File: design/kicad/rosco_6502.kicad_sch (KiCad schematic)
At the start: 54 parts, among them IC1 W65C02SxP, IC2 ATF22V10C-7PX, IC3 XR68C681CJTR-F, IC4 NE555P, IC5 ATF22V10C-7PX, J1 UART_A, J2 UART_B, J3 Conn_01x06, J4 Conn_01x01_Male, J5 Conn_02x18_Odd_Even, J6 Conn_01x02_Male, Q1 3.6864MHz, SW1 SW_DPST, U1 AS6C4008-55PCN, U2 AS6C62256-55PCN, U3 AT28C64B-15PU, U4 74HCT174, X1 14MHz

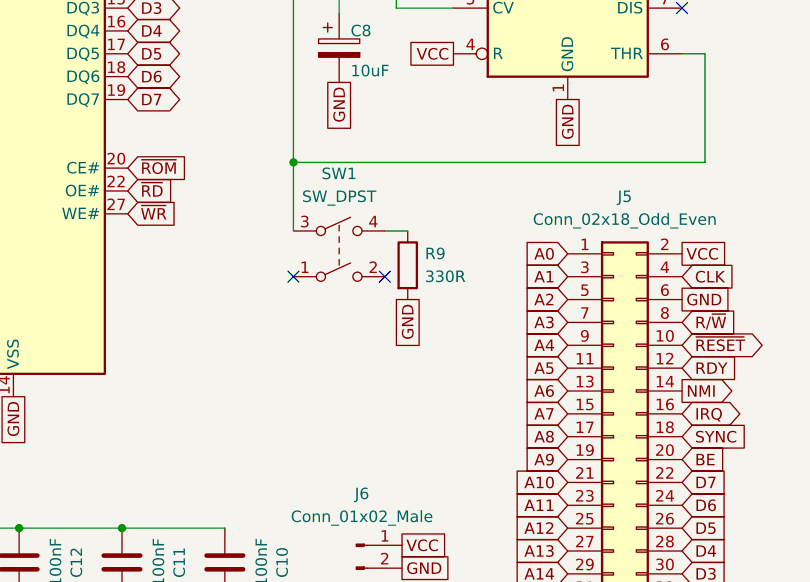
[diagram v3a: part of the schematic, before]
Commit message: Fix incorrect button symbol
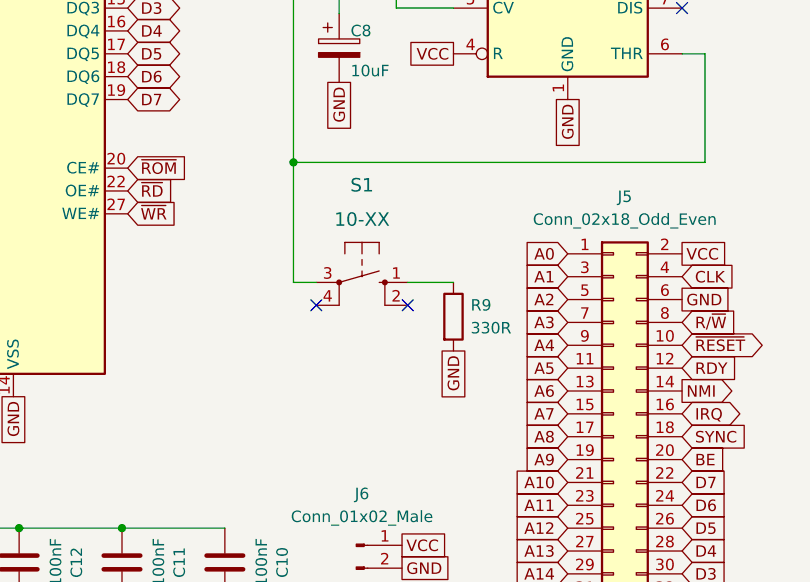
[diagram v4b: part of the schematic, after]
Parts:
- removed SW1: SW_DPST, rosco_6502:B3F-10XX, symbol Switch:SW_DPST
- added S1: 10-XX, rosco_6502:B3F-10XX, symbol rosco_6502:10-XX
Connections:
- net at C8.1, IC4.2 (TR), IC4.6 (THR)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: now also S1.3 (P)
- net at R9.1: now also S1.1 (S)
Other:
- moved on the sheet: R9
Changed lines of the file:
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@@
   (junction (at 195.58 92.71) (diameter 0) (color 0 0 0 0)
   )
-  (no_connect (at 226.06 64.77))
-  (no_connect (at 236.22 64.77))
+  (no_connect (at 228.6 67.945))
+  (no_connect (at 238.76 67.945))
   (no_connect (at 269.24 34.925))
   (no_connect (at 106.68 125.095))
@@
     (stroke (width 0) (type default) (color 0 0 0 0))
   )
-  (wire (pts (xy 226.06 59.69) (xy 226.06 52.07))
+  (wire (pts (xy 226.06 52.07) (xy 226.06 65.405))
     (stroke (width 0) (type default) (color 0 0 0 0))
   )
@@
     (stroke (width 0) (type default) (color 0 0 0 0))
   )
+  (wire (pts (xy 228.6 65.405) (xy 226.06 65.405))
+    (stroke (width 0) (type default) (color 0 0 0 0))
+  )
   (wire (pts (xy 271.78 52.07) (xy 226.06 52.07))
     (stroke (width 0) (type default) (color 0 0 0 0))
@@
     (stroke (width 0) (type default) (color 0 0 0 0))
   )
-  (wire (pts (xy 236.22 59.69) (xy 238.76 59.69))
+  (wire (pts (xy 238.76 65.405) (xy 243.84 65.405))
     (stroke (width 0) (type default) (color 0 0 0 0))
   )
@@
     )
   )
-  (global_label "GND" (shape passive) (at 238.76 67.31 270) (fields_autoplaced)
+  (global_label "GND" (shape passive) (at 243.84 73.025 270) (fields_autoplaced)
     (effects (font (size 1.27 1.27)) (justify right))
-    (property "Intersheet References" "${INTERSHEET_REFS}" (id 0) (at 238.6806 73.5936 90)
+    (property "Intersheet References" "${INTERSHEET_REFS}" (id 0) (at 243.7606 79.3086 90)
       (effects (font (size 1.27 1.27)) (justify right) hide)
     )
@@
     (pin "2")
   )
-  (symbol (lib_id "Switch:SW_DPST") (at 231.14 62.23 0) (unit 1)
-    (in_bom yes) (on_board yes) (fields_autoplaced)
-    (property "Reference" "SW1" (id 0) (at 231.14 53.34 0))
-    (property "Value" "SW_DPST" (id 1) (at 231.14 55.88 0))
-    (property "Footprint" "rosco_6502:B3F-10XX" (id 2) (at 231.14 62.23 0)
-      (effects (font (size 1.27 1.27)) hide)
-    )
-    (property "Datasheet" "~" (id 3) (at 231.14 62.23 0)
-      (effects (font (size 1.27 1.27)) hide)
-    )
-    (pin "1")
-    (pin "2")
-    (pin "3")
-    (pin "4")
-  )
   (symbol (lib_id "Connector_Generic:Conn_02x18_Odd_Even") (at 261.62 82.55 0) (unit 1)
     (in_bom yes) (on_board yes) (fields_autoplaced)
@@
     (pin "6")
   )
-  (symbol (lib_id "Device:R") (at 238.76 63.5 0) (unit 1)
+  (symbol (lib_id "Device:R") (at 243.84 69.215 0) (unit 1)
     (in_bom yes) (on_board yes)
-    (property "Reference" "R9" (id 0) (at 240.665 62.23 0)
+    (property "Reference" "R9" (id 0) (at 245.745 67.945 0)
       (effects (font (size 1.27 1.27)) (justify left))
     )
-    (property "Value" "330R" (id 1) (at 240.665 64.77 0)
+    (property "Value" "330R" (id 1) (at 245.745 70.485 0)
       (effects (font (size 1.27 1.27)) (justify left))
     )
-    (property "Footprint" "Resistor_THT:R_Axial_DIN0207_L6.3mm_D2.5mm_P10.16mm_Horizontal" (id 2) (at 236.982 63.5 90)
+    (property "Footprint" "Resistor_THT:R_Axial_DIN0207_L6.3mm_D2.5mm_P10.16mm_Horizontal" (id 2) (at 242.062 69.215 90)
       (effects (font (size 1.27 1.27)) hide)
     )
-    (property "Datasheet" "~" (id 3) (at 238.76 63.5 0)
+    (property "Datasheet" "~" (id 3) (at 243.84 69.215 0)
       (effects (font (size 1.27 1.27)) hide)
     )
@@
     (pin "2")
   )
+  (symbol (lib_id "rosco_6502:10-XX") (at 233.68 65.405 270) (unit 1)
+    (in_bom yes) (on_board yes) (fields_autoplaced)
+    (property "Reference" "S1" (id 0) (at 233.68 54.61 90)
+      (effects (font (size 1.4986 1.4986)))
+    )
+    (property "Value" "10-XX" (id 1) (at 233.68 58.42 90)
+      (effects (font (size 1.4986 1.4986)))
+    )
+    (property "Footprint" "rosco_6502:B3F-10XX" (id 2) (at 233.68 65.405 0)
+      (effects (font (size 1.27 1.27)) hide)
+    )
+    (property "Datasheet" "" (id 3) (at 233.68 65.405 0)
+      (effects (font (size 1.27 1.27)) hide)
+    )
+    (pin "1")
+    (pin "2")
+    (pin "3")
+    (pin "4")
+  )
   (symbol (lib_id "rosco_6502:GAL22V10") (at 153.67 135.255 0) (unit 1)
     (in_bom yes) (on_board yes) (fields_autoplaced)
@@
       (reference "R11") (unit 1) (value "3K3") (footprint "Resistor_THT:R_Axial_DIN0207_L6.3mm_D2.5mm_P10.16mm_Horizontal")
     )
-    (path "/0d61b5ac-4ff5-4ae4-a1de-fa50189d2dac"
-      (reference "SW1") (unit 1) (value "SW_DPST") (footprint "rosco_6502:B3F-10XX")
+    (path "/8a9d55c4-cad3-46c0-840f-2a6683619b87"
+      (reference "S1") (unit 1) (value "10-XX") (footprint "rosco_6502:B3F-10XX")
     )
     (path "/a19ecf22-39ce-40ef-8344-8635412e5bee"

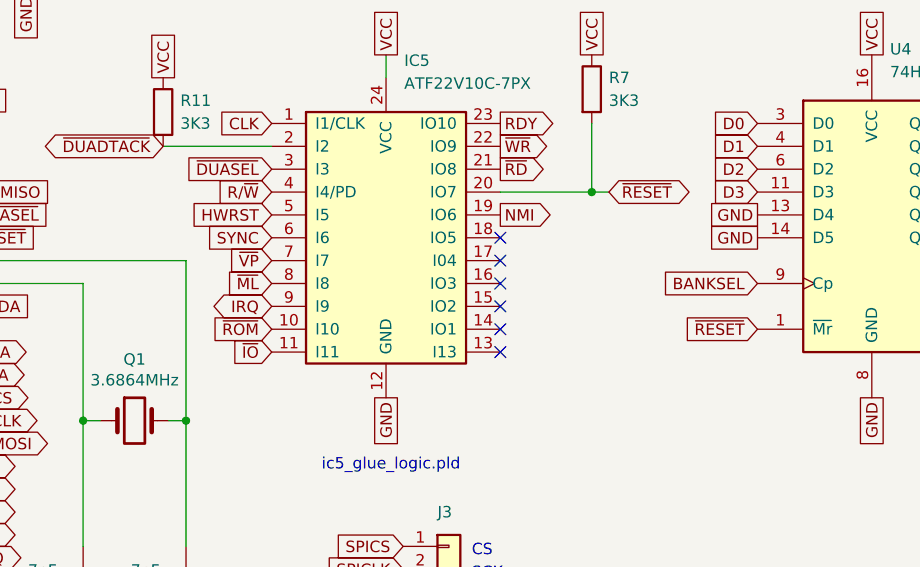
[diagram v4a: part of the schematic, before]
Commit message: Stretch timing for BANKSEL via glue
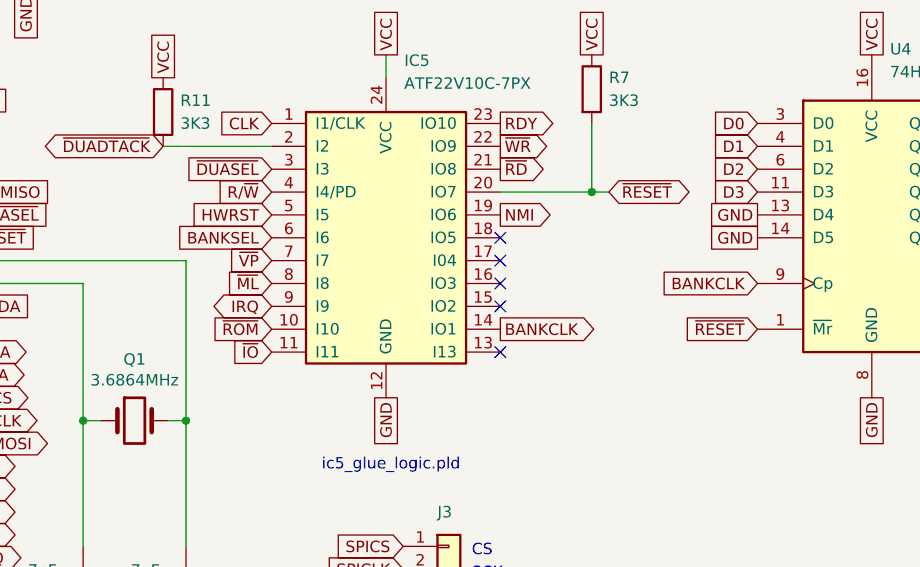
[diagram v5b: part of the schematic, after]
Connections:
- net BANKSEL: now also IC5.6 (I6); no longer U4.9 (Cp)
- net SYNC: no longer IC5.6 (I6)
- net BANKCLK: now reaches IC5.14 (IO1)
- net BANKCLK: now also U4.9 (Cp)
- no-connect marks 16 -> 15
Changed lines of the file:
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@@
   (no_connect (at 220.345 135.255))
   (no_connect (at 166.37 142.875))
-  (no_connect (at 166.37 145.415))
   (no_connect (at 166.37 147.955))
   (no_connect (at 166.37 140.335))
@@
     )
   )
+  (global_label "BANKSEL" (shape input) (at 140.97 135.255 180) (fields_autoplaced)
+    (effects (font (size 1.27 1.27)) (justify right))
+    (property "Intersheet References" "${INTERSHEET_REFS}" (id 0) (at 130.2112 135.1756 0)
+      (effects (font (size 1.27 1.27)) (justify right) hide)
+    )
+  )
   (global_label "~{ROM}" (shape output) (at 268.605 125.095 0) (fields_autoplaced)
     (effects (font (size 1.27 1.27)) (justify left))
@@
     )
   )
+  (global_label "BANKCLK" (shape input) (at 194.945 140.335 180) (fields_autoplaced)
+    (effects (font (size 1.27 1.27)) (justify right))
+    (property "Intersheet References" "${INTERSHEET_REFS}" (id 0) (at 184.0048 140.4144 0)
+      (effects (font (size 1.27 1.27)) (justify right) hide)
+    )
+  )
   (global_label "D5" (shape bidirectional) (at 81.28 83.185 0) (fields_autoplaced)
     (effects (font (size 1.27 1.27)) (justify left))
@@
     )
   )
-  (global_label "BANKSEL" (shape input) (at 194.945 140.335 180) (fields_autoplaced)
-    (effects (font (size 1.27 1.27)) (justify right))
-    (property "Intersheet References" "${INTERSHEET_REFS}" (id 0) (at 184.1862 140.2556 0)
-      (effects (font (size 1.27 1.27)) (justify right) hide)
-    )
-  )
   (global_label "A5" (shape input) (at 182.245 40.005 180) (fields_autoplaced)
     (effects (font (size 1.27 1.27)) (justify right))
@@
     )
   )
+  (global_label "BANKCLK" (shape output) (at 166.37 145.415 0) (fields_autoplaced)
+    (effects (font (size 1.27 1.27)) (justify left))
+    (property "Intersheet References" "${INTERSHEET_REFS}" (id 0) (at 177.3102 145.3356 0)
+      (effects (font (size 1.27 1.27)) (justify left) hide)
+    )
+  )
   (global_label "GND" (shape passive) (at 26.67 175.895 0) (fields_autoplaced)
     (effects (font (size 1.27 1.27)) (justify left))
@@
     )
   )
-  (global_label "SYNC" (shape input) (at 140.97 135.255 180) (fields_autoplaced)
-    (effects (font (size 1.27 1.27)) (justify right))
-    (property "Intersheet References" "${INTERSHEET_REFS}" (id 0) (at 133.6583 135.1756 0)
-      (effects (font (size 1.27 1.27)) (justify right) hide)
-    )
-  )
